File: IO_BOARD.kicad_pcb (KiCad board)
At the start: 4 copper layers, 18 x 23.5 mm, 5 parts, among them J2 TYPE-C-31-M-12

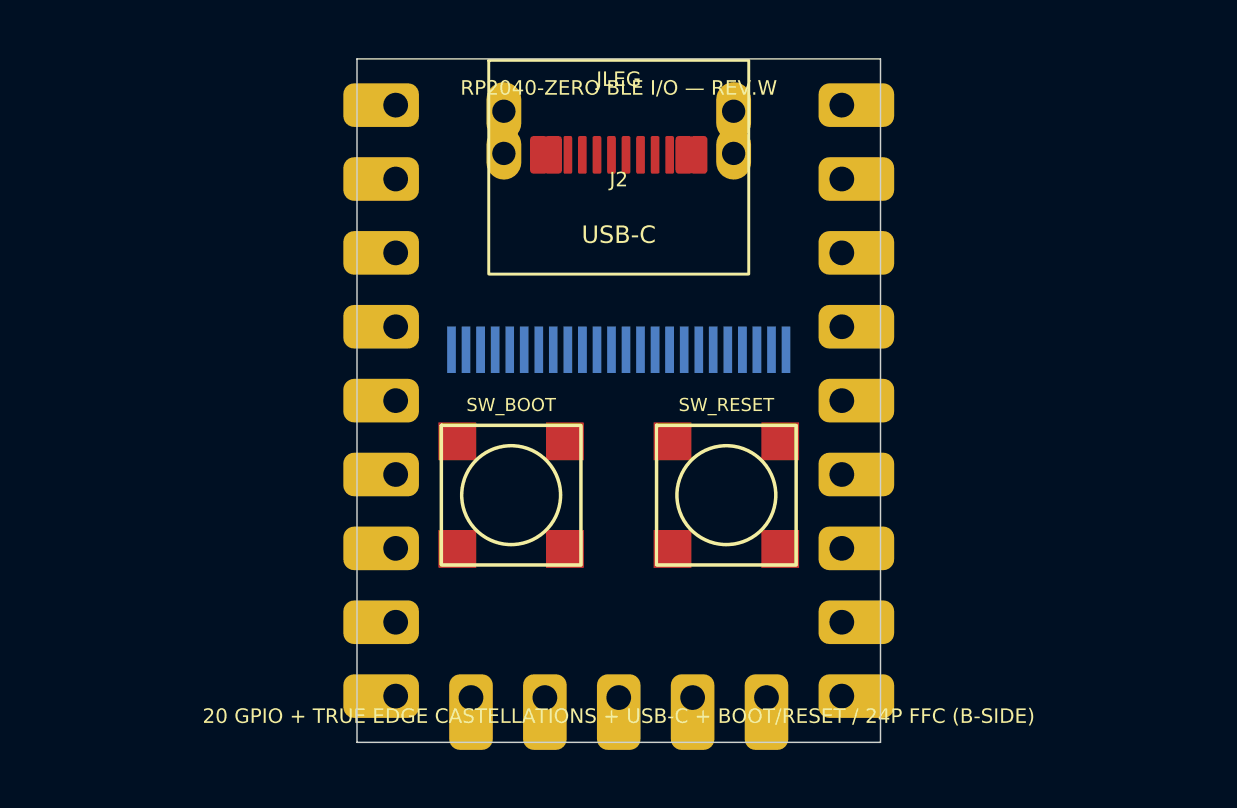
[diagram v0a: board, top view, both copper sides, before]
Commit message: Add 24P vertical FFC on front side
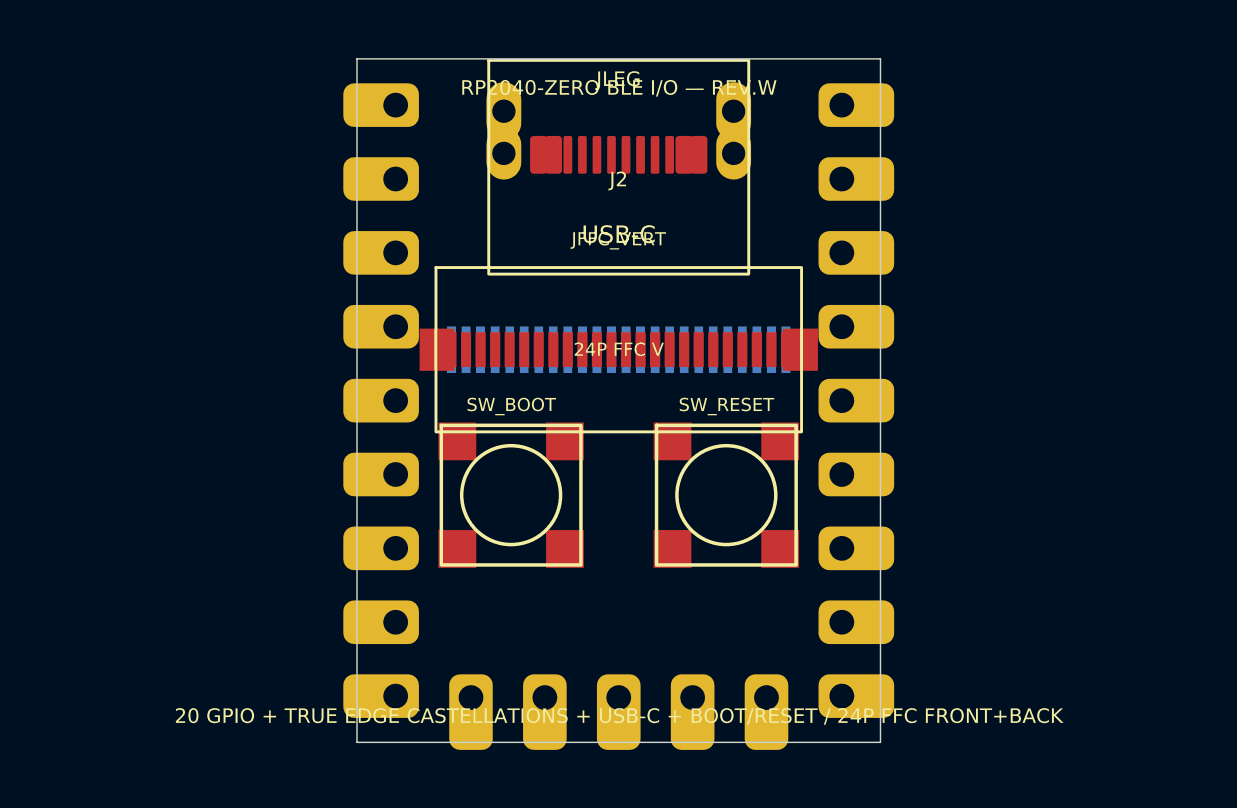
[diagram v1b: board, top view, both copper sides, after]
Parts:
- added JFFC_VERT: FH40-24S-0.5SV, FH40-24S-0.5SV, F.Cu at (9.00, 10.0)
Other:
- board text added: "20 GPIO + TRUE EDGE CASTELLATIONS + USB-C + BOOT/RESET / 24P FFC FRONT+BACK"
- board text removed: "20 GPIO + TRUE EDGE CASTELLATIONS + USB-C + BOOT/RESET / 24P FFC (B-SIDE)"
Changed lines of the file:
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@@
  (gr_rect (start 0 0) (end 18 23.5) (stroke (width 0.05) (type default)) (fill none) (layer "Edge.Cuts"))
  (gr_text "RP2040-ZERO BLE I/O — REV.W" (at 9 1.0) (layer "F.SilkS") (effects (font (size 0.5 0.5) (thickness 0.1))))
- (gr_text "20 GPIO + TRUE EDGE CASTELLATIONS + USB-C + BOOT/RESET / 24P FFC (B-SIDE)" (at 9 22.6) (layer "F.SilkS") (effects (font (size 0.5 0.5) (thickness 0.1))))
+ (gr_text "20 GPIO + TRUE EDGE CASTELLATIONS + USB-C + BOOT/RESET / 24P FFC FRONT+BACK" (at 9 22.6) (layer "F.SilkS") (effects (font (size 0.5 0.5) (thickness 0.1))))
  (footprint "RP2040-Zero-THT-Interface" (layer "F.Cu") (at 0 0)
   (fp_text reference "JLEG" (at 9 0.7) (layer "F.SilkS") (effects (font (size 0.5 0.5) (thickness 0.08))))
@@
   (pad "S4" thru_hole oval (at 3.95 3.00) (size 1.20 1.80) (drill 0.80) (layers "*.Cu" "*.Mask"))
  )
+ (footprint "FH40-24S-0.5SV" (layer "F.Cu") (at 9 10.0)
+  (fp_text reference "JFFC_VERT" (at 0 -3.8) (layer "F.SilkS")
+    (effects (font (size 0.45 0.45) (thickness 0.08)))
+  )
+  (fp_text value "FH40-24S-0.5SV" (at 0 3.8) (layer "F.Fab") hide
+    (effects (font (size 0.8 0.8) (thickness 0.12)))
+  )
+  (fp_rect (start -6.285 -2.825) (end 6.285 2.825)
+    (stroke (width 0.10) (type default)) (fill none) (layer "F.SilkS"))
+  (fp_rect (start -6.35 -2.9) (end 6.35 2.9)
+    (stroke (width 0.05) (type default)) (fill none) (layer "F.CrtYd"))
+  (fp_text user "24P FFC V" (at 0 0) (layer "F.SilkS")
+    (effects (font (size 0.45 0.45) (thickness 0.08)))
+  )
+  (pad "1" smd rect (at -5.75 0) (size 0.35 1.20) (layers "F.Cu" "F.Paste" "F.Mask") (net 1 "GPIO0"))
+  (pad "2" smd rect (at -5.25 0) (size 0.35 1.20) (layers "F.Cu" "F.Paste" "F.Mask") (net 2 "GPIO1"))
+  (pad "3" smd rect (at -4.75 0) (size 0.35 1.20) (layers "F.Cu" "F.Paste" "F.Mask") (net 3 "GPIO2"))
+  (pad "4" smd rect (at -4.25 0) (size 0.35 1.20) (layers "F.Cu" "F.Paste" "F.Mask") (net 4 "GPIO3"))
+  (pad "5" smd rect (at -3.75 0) (size 0.35 1.20) (layers "F.Cu" "F.Paste" "F.Mask") (net 5 "GPIO4"))
+  (pad "6" smd rect (at -3.25 0) (size 0.35 1.20) (layers "F.Cu" "F.Paste" "F.Mask") (net 6 "GPIO5"))
+  (pad "7" smd rect (at -2.75 0) (size 0.35 1.20) (layers "F.Cu" "F.Paste" "F.Mask") (net 7 "GPIO6"))
+  (pad "8" smd rect (at -2.25 0) (size 0.35 1.20) (layers "F.Cu" "F.Paste" "F.Mask") (net 8 "GPIO7"))
+  (pad "9" smd rect (at -1.75 0) (size 0.35 1.20) (layers "F.Cu" "F.Paste" "F.Mask") (net 9 "GPIO8"))
+  (pad "10" smd rect (at -1.25 0) (size 0.35 1.20) (layers "F.Cu" "F.Paste" "F.Mask") (net 10 "GPIO9"))
+  (pad "11" smd rect (at -0.75 0) (size 0.35 1.20) (layers "F.Cu" "F.Paste" "F.Mask") (net 11 "GPIO10"))
+  (pad "12" smd rect (at -0.25 0) (size 0.35 1.20) (layers "F.Cu" "F.Paste" "F.Mask") (net 12 "GPIO11"))
+  (pad "13" smd rect (at 0.25 0) (size 0.35 1.20) (layers "F.Cu" "F.Paste" "F.Mask") (net 13 "GPIO12"))
+  (pad "14" smd rect (at 0.75 0) (size 0.35 1.20) (layers "F.Cu" "F.Paste" "F.Mask") (net 14 "GPIO13"))
+  (pad "15" smd rect (at 1.25 0) (size 0.35 1.20) (layers "F.Cu" "F.Paste" "F.Mask") (net 15 "GPIO14"))
+  (pad "16" smd rect (at 1.75 0) (size 0.35 1.20) (layers "F.Cu" "F.Paste" "F.Mask") (net 16 "GPIO15"))
+  (pad "17" smd rect (at 2.25 0) (size 0.35 1.20) (layers "F.Cu" "F.Paste" "F.Mask") (net 17 "GPIO26"))
+  (pad "18" smd rect (at 2.75 0) (size 0.35 1.20) (layers "F.Cu" "F.Paste" "F.Mask") (net 18 "GPIO27"))
+  (pad "19" smd rect (at 3.25 0) (size 0.35 1.20) (layers "F.Cu" "F.Paste" "F.Mask") (net 19 "GPIO28"))
+  (pad "20" smd rect (at 3.75 0) (size 0.35 1.20) (layers "F.Cu" "F.Paste" "F.Mask") (net 20 "GPIO29"))
+  (pad "21" smd rect (at 4.25 0) (size 0.35 1.20) (layers "F.Cu" "F.Paste" "F.Mask") (net 21 "3V3"))
+  (pad "22" smd rect (at 4.75 0) (size 0.35 1.20) (layers "F.Cu" "F.Paste" "F.Mask") (net 22 "GND"))
+  (pad "23" smd rect (at 5.25 0) (size 0.35 1.20) (layers "F.Cu" "F.Paste" "F.Mask") (net 23 "VSYS"))
+  (pad "24" smd rect (at 5.75 0) (size 0.35 1.20) (layers "F.Cu" "F.Paste" "F.Mask") (net 24 "USB_VBUS"))
+  (pad "25" smd rect (at -6.25 0) (size 1.20 1.45) (layers "F.Cu" "F.Paste" "F.Mask"))
+  (pad "26" smd rect (at 6.25 0) (size 1.20 1.45) (layers "F.Cu" "F.Paste" "F.Mask"))
+ )
  (footprint "FH34SRJ-24S-0.5SH(50)" (layer "B.Cu") (at 9 10.0)

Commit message: Use castellated SMD RP2040-Zero mechanical master
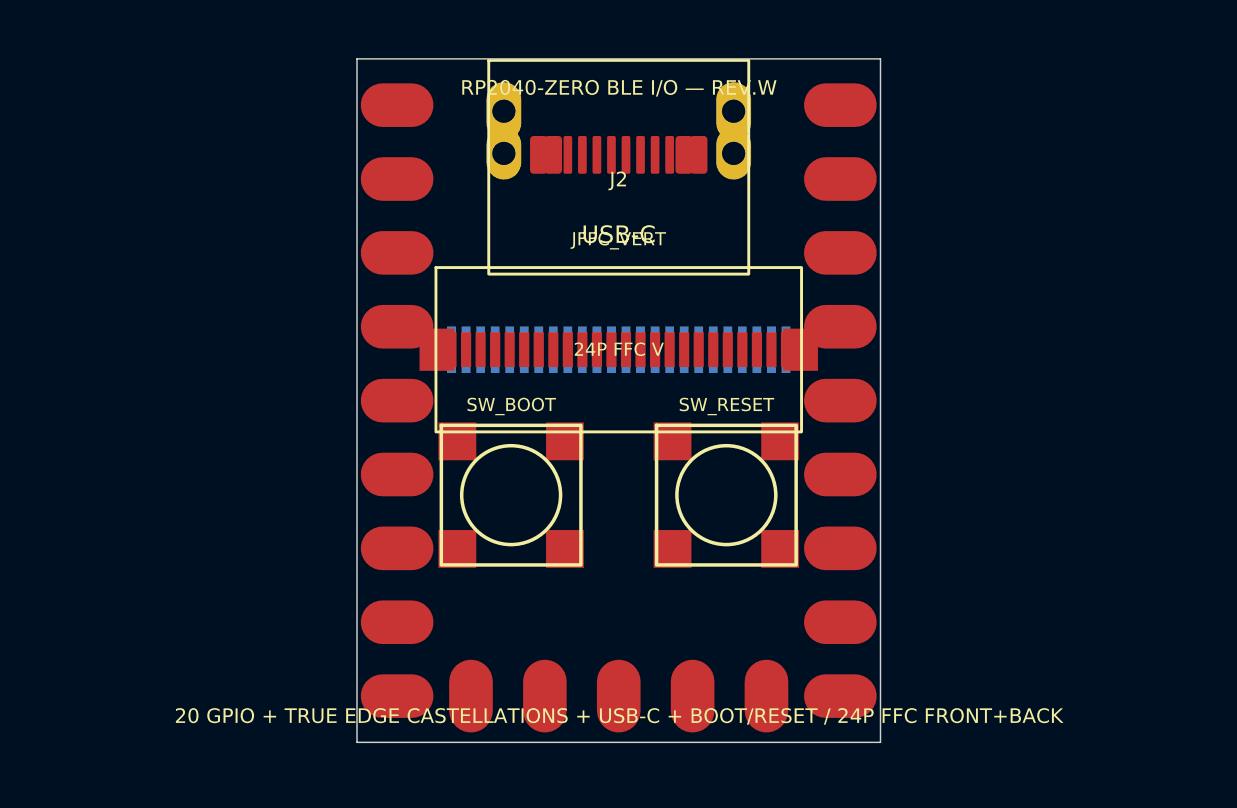
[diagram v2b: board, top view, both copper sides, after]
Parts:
- removed the JLEG at (0.00, 0.00)
- added JLEG: RP2040-Zero castellated mechanical master, RP2040-Zero-Castellated-Master, F.Cu at (0.00, 0.00)
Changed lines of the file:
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@@
  (gr_text "RP2040-ZERO BLE I/O — REV.W" (at 9 1.0) (layer "F.SilkS") (effects (font (size 0.5 0.5) (thickness 0.1))))
  (gr_text "20 GPIO + TRUE EDGE CASTELLATIONS + USB-C + BOOT/RESET / 24P FFC FRONT+BACK" (at 9 22.6) (layer "F.SilkS") (effects (font (size 0.5 0.5) (thickness 0.1))))
- (footprint "RP2040-Zero-THT-Interface" (layer "F.Cu") (at 0 0)
-  (fp_text reference "JLEG" (at 9 0.7) (layer "F.SilkS") (effects (font (size 0.5 0.5) (thickness 0.08))))
-  (fp_text value "RP2040-Zero-THT mechanical master" (at 9 22.8) (layer "F.Fab") hide (effects (font (size 0.8 0.8) (thickness 0.12))))
-  (pad "0" thru_hole roundrect (at 16.67 1.59 180) (size 2.60 1.50) (drill 0.85 (offset -0.50 0)) (layers "*.Cu" "*.Mask") (roundrect_rratio 0.25) (net 1 "GPIO0"))
-  (pad "1" thru_hole roundrect (at 16.67 4.13 180) (size 2.60 1.50) (drill 0.85 (offset -0.50 0)) (layers "*.Cu" "*.Mask") (roundrect_rratio 0.25) (net 2 "GPIO1"))
-  (pad "2" thru_hole roundrect (at 16.67 6.67 180) (size 2.60 1.50) (drill 0.85 (offset -0.50 0)) (layers "*.Cu" "*.Mask") (roundrect_rratio 0.25) (net 3 "GPIO2"))
-  (pad "3" thru_hole roundrect (at 16.67 9.21 180) (size 2.60 1.50) (drill 0.85 (offset -0.50 0)) (layers "*.Cu" "*.Mask") (roundrect_rratio 0.25) (net 4 "GPIO3"))
-  (pad "4" thru_hole roundrect (at 16.67 11.75 180) (size 2.60 1.50) (drill 0.85 (offset -0.50 0)) (layers "*.Cu" "*.Mask") (roundrect_rratio 0.25) (net 5 "GPIO4"))
-  (pad "5" thru_hole roundrect (at 16.67 14.29 180) (size 2.60 1.50) (drill 0.85 (offset -0.50 0)) (layers "*.Cu" "*.Mask") (roundrect_rratio 0.25) (net 6 "GPIO5"))
-  (pad "6" thru_hole roundrect (at 16.67 16.83 180) (size 2.60 1.50) (drill 0.85 (offset -0.50 0)) (layers "*.Cu" "*.Mask") (roundrect_rratio 0.25) (net 7 "GPIO6"))
-  (pad "7" thru_hole roundrect (at 16.67 19.37 180) (size 2.60 1.50) (drill 0.85 (offset -0.50 0)) (layers "*.Cu" "*.Mask") (roundrect_rratio 0.25) (net 8 "GPIO7"))
-  (pad "8" thru_hole roundrect (at 16.67 21.91 180) (size 2.60 1.50) (drill 0.85 (offset -0.50 0)) (layers "*.Cu" "*.Mask") (roundrect_rratio 0.25) (net 9 "GPIO8"))
-  (pad "9" thru_hole roundrect (at 14.08 21.96 90) (size 2.60 1.50) (drill 0.85 (offset -0.50 0)) (layers "*.Cu" "*.Mask") (roundrect_rratio 0.25) (net 10 "GPIO9"))
-  (pad "10" thru_hole roundrect (at 11.54 21.96 90) (size 2.60 1.50) (drill 0.85 (offset -0.50 0)) (layers "*.Cu" "*.Mask") (roundrect_rratio 0.25) (net 11 "GPIO10"))
-  (pad "11" thru_hole roundrect (at 9.00 21.96 90) (size 2.60 1.50) (drill 0.85 (offset -0.50 0)) (layers "*.Cu" "*.Mask") (roundrect_rratio 0.25) (net 12 "GPIO11"))
-  (pad "12" thru_hole roundrect (at 6.46 21.96 90) (size 2.60 1.50) (drill 0.85 (offset -0.50 0)) (layers "*.Cu" "*.Mask") (roundrect_rratio 0.25) (net 13 "GPIO12"))
-  (pad "13" thru_hole roundrect (at 3.92 21.96 90) (size 2.60 1.50) (drill 0.85 (offset -0.50 0)) (layers "*.Cu" "*.Mask") (roundrect_rratio 0.25) (net 14 "GPIO13"))
-  (pad "14" thru_hole roundrect (at 1.33 21.91 0) (size 2.60 1.50) (drill 0.85 (offset -0.50 0)) (layers "*.Cu" "*.Mask") (roundrect_rratio 0.25) (net 15 "GPIO14"))
-  (pad "15" thru_hole roundrect (at 1.33 19.37 0) (size 2.60 1.50) (drill 0.85 (offset -0.50 0)) (layers "*.Cu" "*.Mask") (roundrect_rratio 0.25) (net 16 "GPIO15"))
-  (pad "16" thru_hole roundrect (at 1.33 16.83 0) (size 2.60 1.50) (drill 0.85 (offset -0.50 0)) (layers "*.Cu" "*.Mask") (roundrect_rratio 0.25) (net 17 "GPIO26"))
-  (pad "17" thru_hole roundrect (at 1.33 14.29 0) (size 2.60 1.50) (drill 0.85 (offset -0.50 0)) (layers "*.Cu" "*.Mask") (roundrect_rratio 0.25) (net 18 "GPIO27"))
-  (pad "18" thru_hole roundrect (at 1.33 11.75 0) (size 2.60 1.50) (drill 0.85 (offset -0.50 0)) (layers "*.Cu" "*.Mask") (roundrect_rratio 0.25) (net 19 "GPIO28"))
-  (pad "19" thru_hole roundrect (at 1.33 9.21 0) (size 2.60 1.50) (drill 0.85 (offset -0.50 0)) (layers "*.Cu" "*.Mask") (roundrect_rratio 0.25) (net 20 "GPIO29"))
-  (pad "20" thru_hole roundrect (at 1.33 6.67 0) (size 2.60 1.50) (drill 0.85 (offset -0.50 0)) (layers "*.Cu" "*.Mask") (roundrect_rratio 0.25) (net 21 "3V3"))
-  (pad "21" thru_hole roundrect (at 1.33 4.13 0) (size 2.60 1.50) (drill 0.85 (offset -0.50 0)) (layers "*.Cu" "*.Mask") (roundrect_rratio 0.25) (net 22 "GND"))
-  (pad "22" thru_hole roundrect (at 1.33 1.59 0) (size 2.60 1.50) (drill 0.85 (offset -0.50 0)) (layers "*.Cu" "*.Mask") (roundrect_rratio 0.25) (net 23 "VSYS"))
+ (footprint "RP2040-Zero-Castellated-Master" (layer "F.Cu") (at 0 0)
+  (fp_text reference "JLEG" (at 9 0.7) (layer "F.SilkS") hide
+    (effects (font (size 0.5 0.5) (thickness 0.08))))
+  (fp_text value "RP2040-Zero castellated mechanical master" (at 9 22.8) (layer "F.Fab") hide
+    (effects (font (size 0.8 0.8) (thickness 0.12))))
+  (pad "0" smd oval (at 16.62 1.59 180) (size 2.50 1.50) (layers "F.Cu" "F.Paste" "F.Mask") (net 1 "GPIO0"))
+  (pad "1" smd oval (at 16.62 4.13 180) (size 2.50 1.50) (layers "F.Cu" "F.Paste" "F.Mask") (net 2 "GPIO1"))
+  (pad "2" smd oval (at 16.62 6.67 180) (size 2.50 1.50) (layers "F.Cu" "F.Paste" "F.Mask") (net 3 "GPIO2"))
+  (pad "3" smd oval (at 16.62 9.21 180) (size 2.50 1.50) (layers "F.Cu" "F.Paste" "F.Mask") (net 4 "GPIO3"))
+  (pad "4" smd oval (at 16.62 11.75 180) (size 2.50 1.50) (layers "F.Cu" "F.Paste" "F.Mask") (net 5 "GPIO4"))
+  (pad "5" smd oval (at 16.62 14.29 180) (size 2.50 1.50) (layers "F.Cu" "F.Paste" "F.Mask") (net 6 "GPIO5"))
+  (pad "6" smd oval (at 16.62 16.83 180) (size 2.50 1.50) (layers "F.Cu" "F.Paste" "F.Mask") (net 7 "GPIO6"))
+  (pad "7" smd oval (at 16.62 19.37 180) (size 2.50 1.50) (layers "F.Cu" "F.Paste" "F.Mask") (net 8 "GPIO7"))
+  (pad "8" smd oval (at 16.62 21.91 180) (size 2.50 1.50) (layers "F.Cu" "F.Paste" "F.Mask") (net 9 "GPIO8"))
+  (pad "9" smd oval (at 14.08 21.91 90) (size 2.50 1.50) (layers "F.Cu" "F.Paste" "F.Mask") (net 10 "GPIO9"))
+  (pad "10" smd oval (at 11.54 21.91 90) (size 2.50 1.50) (layers "F.Cu" "F.Paste" "F.Mask") (net 11 "GPIO10"))
+  (pad "11" smd oval (at 9.00 21.91 90) (size 2.50 1.50) (layers "F.Cu" "F.Paste" "F.Mask") (net 12 "GPIO11"))
+  (pad "12" smd oval (at 6.46 21.91 90) (size 2.50 1.50) (layers "F.Cu" "F.Paste" "F.Mask") (net 13 "GPIO12"))
+  (pad "13" smd oval (at 3.92 21.91 90) (size 2.50 1.50) (layers "F.Cu" "F.Paste" "F.Mask") (net 14 "GPIO13"))
+  (pad "14" smd oval (at 1.38 21.91 0) (size 2.50 1.50) (layers "F.Cu" "F.Paste" "F.Mask") (net 15 "GPIO14"))
+  (pad "15" smd oval (at 1.38 19.37 0) (size 2.50 1.50) (layers "F.Cu" "F.Paste" "F.Mask") (net 16 "GPIO15"))
+  (pad "16" smd oval (at 1.38 16.83 0) (size 2.50 1.50) (layers "F.Cu" "F.Paste" "F.Mask") (net 17 "GPIO26"))
+  (pad "17" smd oval (at 1.38 14.29 0) (size 2.50 1.50) (layers "F.Cu" "F.Paste" "F.Mask") (net 18 "GPIO27"))
+  (pad "18" smd oval (at 1.38 11.75 0) (size 2.50 1.50) (layers "F.Cu" "F.Paste" "F.Mask") (net 19 "GPIO28"))
+  (pad "19" smd oval (at 1.38 9.21 0) (size 2.50 1.50) (layers "F.Cu" "F.Paste" "F.Mask") (net 20 "GPIO29"))
+  (pad "20" smd oval (at 1.38 6.67 0) (size 2.50 1.50) (layers "F.Cu" "F.Paste" "F.Mask") (net 21 "3V3"))
+  (pad "21" smd oval (at 1.38 4.13 0) (size 2.50 1.50) (layers "F.Cu" "F.Paste" "F.Mask") (net 22 "GND"))
+  (pad "22" smd oval (at 1.38 1.59 0) (size 2.50 1.50) (layers "F.Cu" "F.Paste" "F.Mask") (net 23 "VSYS"))
  )
 (footprint "TYPE-C-31-M-12" (layer "F.Cu") (at 9.0 0.25)
